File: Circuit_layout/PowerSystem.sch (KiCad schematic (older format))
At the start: 19 parts, among them U13 PDQ10-D, U14 PDQ15-D, U18 PDQ6-D

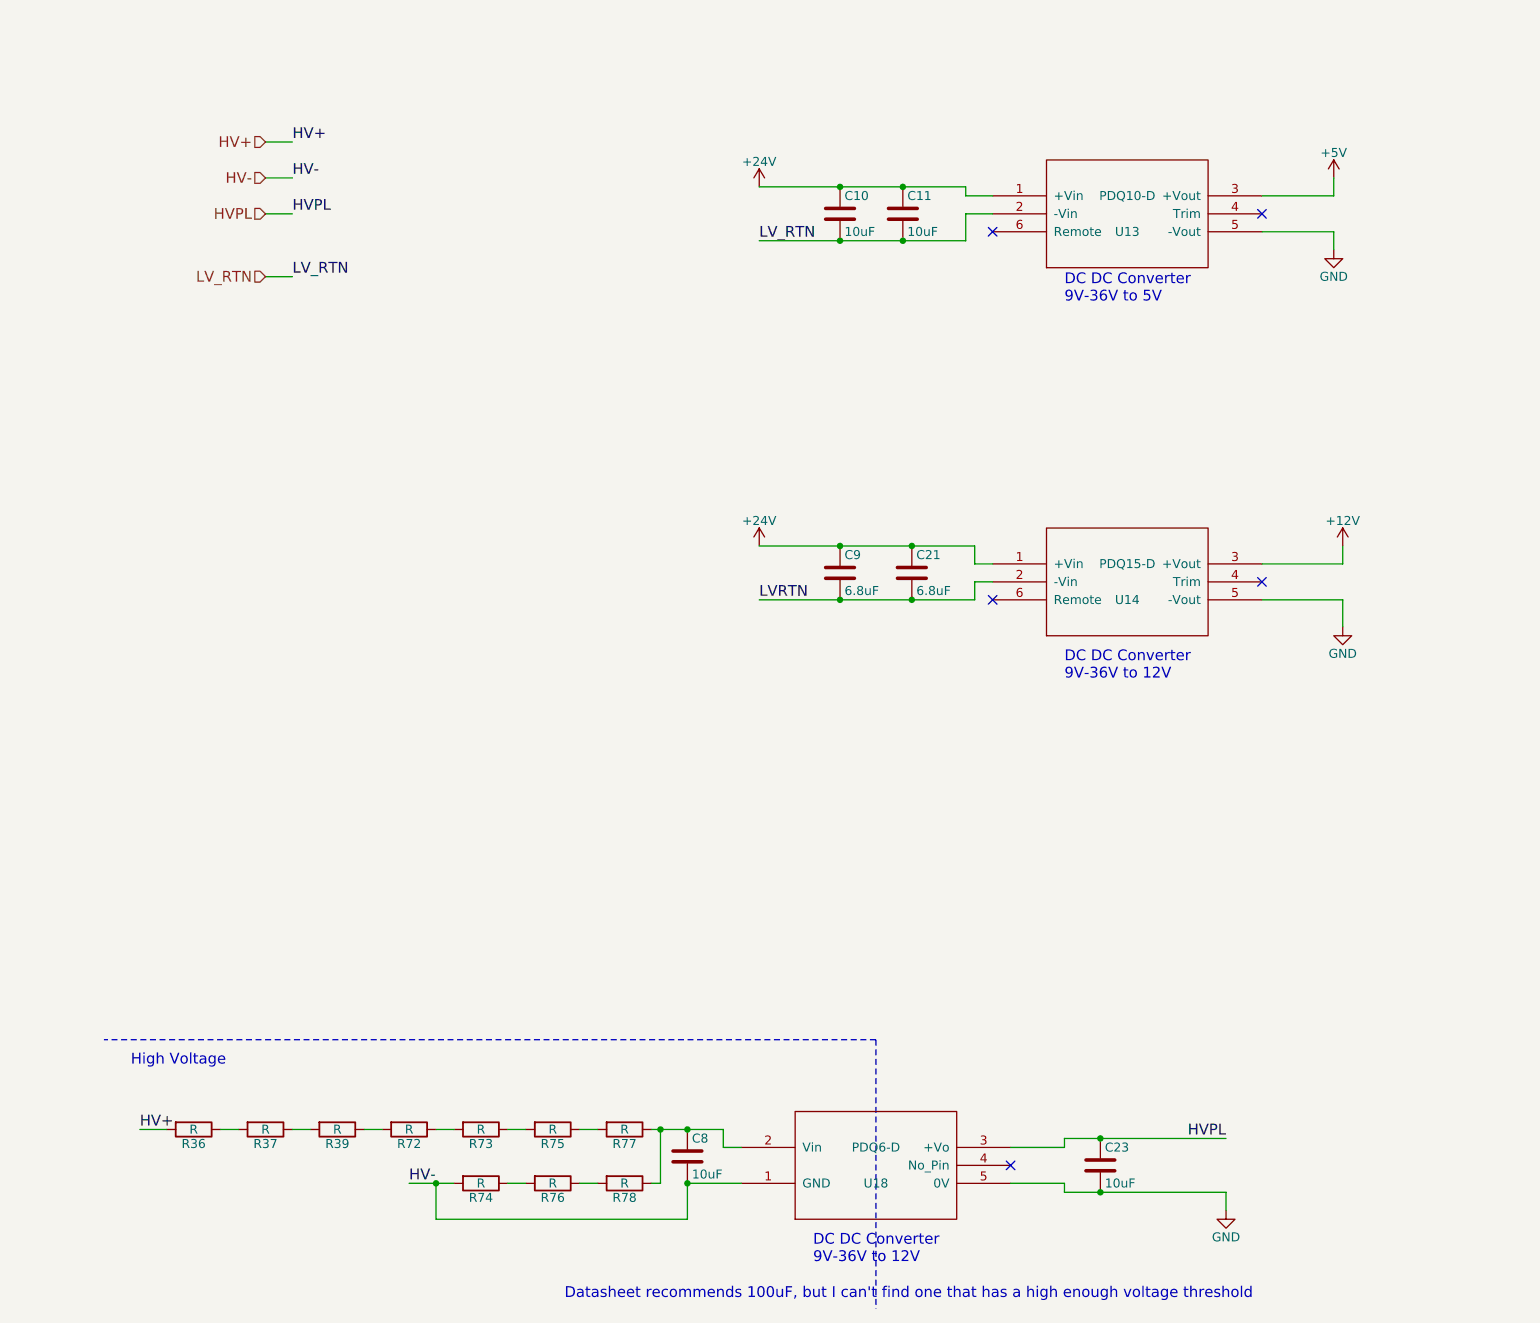
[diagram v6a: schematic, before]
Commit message: cleaned up sch, added bypass pass. no net warnings
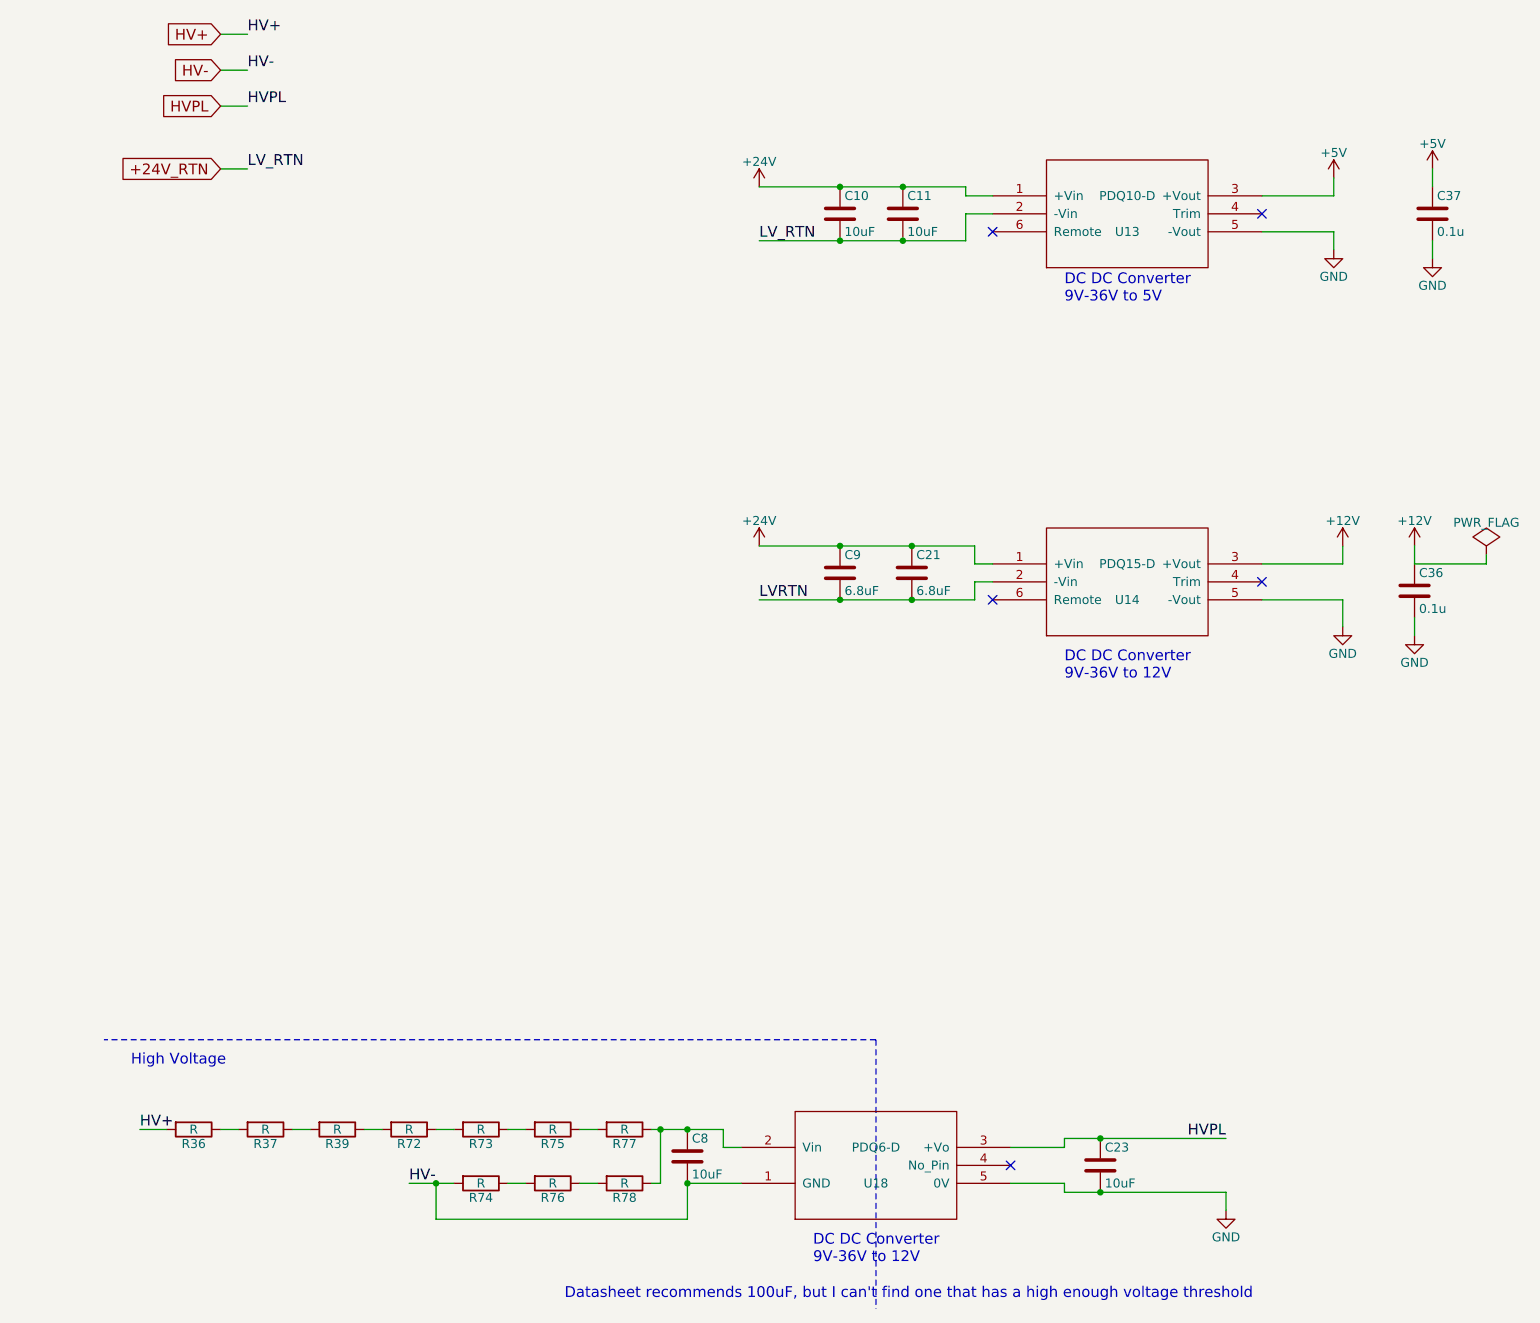
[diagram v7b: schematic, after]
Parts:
- added C36, C37: 0.1u, Capacitors_SMD:C_0805_HandSoldering, symbol C
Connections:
- net +12V: now also C36.1
- net +5V: now also C37.1
- net GND: now also C36.2, C37.2
- net LV_RTN renamed +24V_RTN
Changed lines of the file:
@@
 EESchema Schematic File Version 2
 LIBS:Circuit_layout-rescue
-LIBS:TSI_KiCad_Lib
 LIBS:TSI_HV_Isolater-cache
 LIBS:74xgxx
@@
 Connection ~ 4550 1550
 $Comp
-L +24V #PWR042
+L +24V #PWR43
 U 1 1 58AF1DB3
 P 4100 3550
-F 0 "#PWR042" H 4100 3400 50  0001 C CNN
+F 0 "#PWR43" H 4100 3400 50  0001 C CNN
 F 1 "+24V" H 4100 3690 50  0000 C CNN
 F 2 "" H 4100 3550 50  0000 C CNN
@@
 $EndComp
 $Comp
-L +24V #PWR043
+L +24V #PWR42
 U 1 1 58AF1DD3
 P 4100 1550
-F 0 "#PWR043" H 4100 1400 50  0001 C CNN
+F 0 "#PWR42" H 4100 1400 50  0001 C CNN
 F 1 "+24V" H 4100 1690 50  0000 C CNN
 F 2 "" H 4100 1550 50  0000 C CNN
@@
 	7300 1600 7300 1500
 $Comp
-L +5V #PWR044
+L +5V #PWR45
 U 1 1 58AF2067
 P 7300 1500
-F 0 "#PWR044" H 7300 1350 50  0001 C CNN
+F 0 "#PWR45" H 7300 1350 50  0001 C CNN
 F 1 "+5V" H 7300 1640 50  0000 C CNN
 F 2 "" H 7300 1500 50  0000 C CNN
@@
 $EndComp
 $Comp
-L +12V #PWR045
+L +12V #PWR47
 U 1 1 58AF208D
 P 7350 3550
-F 0 "#PWR045" H 7350 3400 50  0001 C CNN
+F 0 "#PWR47" H 7350 3400 50  0001 C CNN
 F 1 "+12V" H 7350 3690 50  0000 C CNN
 F 2 "" H 7350 3550 50  0000 C CNN
@@
 	7300 1800 7300 1900
 $Comp
-L GND #PWR046
+L GND #PWR46
 U 1 1 58AF2561
 P 7300 1900
-F 0 "#PWR046" H 7300 1650 50  0001 C CNN
+F 0 "#PWR46" H 7300 1650 50  0001 C CNN
 F 1 "GND" H 7300 1750 50  0000 C CNN
 F 2 "" H 7300 1900 50  0000 C CNN
@@
 	7350 3850 7350 4000
 $Comp
-L GND #PWR047
+L GND #PWR48
 U 1 1 58AF25AA
 P 7350 4000
-F 0 "#PWR047" H 7350 3750 50  0001 C CNN
+F 0 "#PWR48" H 7350 3750 50  0001 C CNN
 F 1 "GND" H 7350 3850 50  0000 C CNN
 F 2 "" H 7350 4000 50  0000 C CNN
@@
 Wire Wire Line
 	800  6800 650  6800
-Text HLabel 1350 1300 0    60   Input ~ 0
+Wire Wire Line
+	1100 700  1250 700
+Wire Wire Line
+	1100 900  1250 900
+Wire Wire Line
+	1100 1100 1250 1100
+Wire Wire Line
+	1100 1450 1250 1450
+Text Label 1250 700  0    60   ~ 0
 HV+
-Text HLabel 1350 1500 0    60   Input ~ 0
+Text Label 1250 900  0    60   ~ 0
 HV-
-Text HLabel 1350 1700 0    60   Input ~ 0
+Text Label 1250 1100 0    60   ~ 0
 HVPL
-Text HLabel 1350 2050 0    60   Input ~ 0
+Text Label 1250 1450 0    60   ~ 0
 LV_RTN
-Wire Wire Line
-	1350 1300 1500 1300
-Wire Wire Line
-	1350 1500 1500 1500
-Wire Wire Line
-	1350 1700 1500 1700
-Wire Wire Line
-	1350 2050 1500 2050
-Text Label 1500 1300 0    60   ~ 0
-HV+
-Text Label 1500 1500 0    60   ~ 0
-HV-
-Text Label 1500 1700 0    60   ~ 0
-HVPL
-Text Label 1500 2050 0    60   ~ 0
-LV_RTN
-$Comp
-L GND #PWR048
+$Comp
+L GND #PWR44
 U 1 1 58BA25F0
 P 6700 7250
-F 0 "#PWR048" H 6700 7000 50  0001 C CNN
+F 0 "#PWR44" H 6700 7000 50  0001 C CNN
 F 1 "GND" H 6700 7100 50  0000 C CNN
 F 2 "" H 6700 7250 50  0000 C CNN
@@
 Text Notes 600  6450 0    60   ~ 0
 High Voltage
+$Comp
+L C C37
+U 1 1 58B9D10D
+P 7850 1700
+F 0 "C37" H 7875 1800 50  0000 L CNN
+F 1 "0.1u" H 7875 1600 50  0000 L CNN
+F 2 "Capacitors_SMD:C_0805_HandSoldering" H 7888 1550 50  0001 C CNN
+F 3 "http://www.kemet.com/Lists/ProductCatalog/Attachments/53/KEM_C1002_X7R_SMD.pdf" H 7850 1700 50  0001 C CNN
+F 4 "399-1168-1-ND" H 7850 1700 60  0001 C CNN "Digikey P/N"
+F 5 "http://www.digikey.com/product-detail/en/kemet/C0805C104K3RACTU/399-1168-1-ND/411443" H 7850 1700 60  0001 C CNN "URL"
+F 6 "C0805C104K3RACTU" H 7850 1700 60  0001 C CNN "Man P/N"
+	1    7850 1700
+	1    0    0    -1
+$EndComp
+$Comp
+L GND #PWR52
+U 1 1 58B9D18E
+P 7850 1950
+F 0 "#PWR52" H 7850 1700 50  0001 C CNN
+F 1 "GND" H 7850 1800 50  0000 C CNN
+F 2 "" H 7850 1950 50  0000 C CNN
+F 3 "" H 7850 1950 50  0000 C CNN
+	1    7850 1950
+	1    0    0    -1
+$EndComp
+$Comp
+L +5V #PWR51
+U 1 1 58B9D1D5
+P 7850 1450
+F 0 "#PWR51" H 7850 1300 50  0001 C CNN
+F 1 "+5V" H 7850 1590 50  0000 C CNN
+F 2 "" H 7850 1450 50  0000 C CNN
+F 3 "" H 7850 1450 50  0000 C CNN
+	1    7850 1450
+	1    0    0    -1
+$EndComp
+Wire Wire Line
+	7850 1450 7850 1550
+Wire Wire Line
+	7850 1950 7850 1850
+$Comp
+L C C36
+U 1 1 58B9D39F
+P 7750 3800
+F 0 "C36" H 7775 3900 50  0000 L CNN
+F 1 "0.1u" H 7775 3700 50  0000 L CNN
+F 2 "Capacitors_SMD:C_0805_HandSoldering" H 7788 3650 50  0001 C CNN
+F 3 "http://www.kemet.com/Lists/ProductCatalog/Attachments/53/KEM_C1002_X7R_SMD.pdf" H 7750 3800 50  0001 C CNN
+F 4 "399-1168-1-ND" H 7750 3800 60  0001 C CNN "Digikey P/N"
+F 5 "http://www.digikey.com/product-detail/en/kemet/C0805C104K3RACTU/399-1168-1-ND/411443" H 7750 3800 60  0001 C CNN "URL"
+F 6 "C0805C104K3RACTU" H 7750 3800 60  0001 C CNN "Man P/N"
+	1    7750 3800
+	1    0    0    -1
+$EndComp
+$Comp
+L GND #PWR50
+U 1 1 58B9D3A5
+P 7750 4050
+F 0 "#PWR50" H 7750 3800 50  0001 C CNN
+F 1 "GND" H 7750 3900 50  0000 C CNN
+F 2 "" H 7750 4050 50  0000 C CNN
+F 3 "" H 7750 4050 50  0000 C CNN
+	1    7750 4050
+	1    0    0    -1
+$EndComp
+Wire Wire Line
+	7750 3550 7750 3650
+Wire Wire Line
+	7750 4050 7750 3950
+$Comp
+L +12V #PWR49
+U 1 1 58B9D62A
+P 7750 3550
+F 0 "#PWR49" H 7750 3400 50  0001 C CNN
+F 1 "+12V" H 7750 3690 50  0000 C CNN
+F 2 "" H 7750 3550 50  0000 C CNN
+F 3 "" H 7750 3550 50  0000 C CNN
+	1    7750 3550
+	1    0    0    -1
+$EndComp
+$Comp
+L PWR_FLAG #FLG3
+U 1 1 58B9E33D
+P 8150 3600
+F 0 "#FLG3" H 8150 3695 50  0001 C CNN
+F 1 "PWR_FLAG" H 8150 3780 50  0000 C CNN
+F 2 "" H 8150 3600 50  0000 C CNN
+F 3 "" H 8150 3600 50  0000 C CNN
+	1    8150 3600
+	1    0    0    -1
+$EndComp
+Wire Wire Line
+	7750 3650 8150 3650
+Wire Wire Line
+	8150 3650 8150 3600
+Text GLabel 1100 700  0    60   Input ~ 0
+HV+
+Text GLabel 1100 900  0    60   Input ~ 0
+HV-
+Text GLabel 1100 1100 0    60   Input ~ 0
+HVPL
+Text GLabel 1100 1450 0    60   Input ~ 0
++24V_RTN
 $EndSCHEMATC

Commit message: took notes on nadovich's proposed changes
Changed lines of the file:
@@
 	5400 3650 5300 3650
 Wire Wire Line
-	5300 3650 5300 3550
-Wire Wire Line
-	5300 3550 4100 3550
+	5300 3550 5300 3650
+Wire Wire Line
+	4100 3550 5300 3550
 Connection ~ 4950 3550
 Connection ~ 4550 3550
@@
 	5400 3750 5300 3750
 Wire Wire Line
-	5300 3750 5300 3850
-Wire Wire Line
-	5300 3850 4100 3850
+	5300 3850 5300 3750
+Wire Wire Line
+	4100 3850 5300 3850
 Connection ~ 4950 3850
 Connection ~ 4550 3850
@@
 	5400 1600 5250 1600
 Wire Wire Line
-	5250 1600 5250 1550
+	5250 1550 5250 1600
 Wire Wire Line
 	5400 1700 5250 1700
 Wire Wire Line
-	5250 1700 5250 1850
-Wire Wire Line
-	5250 1850 4100 1850
+	5250 1850 5250 1700
+Wire Wire Line
+	4100 1850 5250 1850
 Connection ~ 4900 1550
 Connection ~ 4900 1850
@@
 	4000 6900 3900 6900
 Wire Wire Line
-	3900 6900 3900 6800
-Wire Wire Line
-	3900 6800 3500 6800
+	3900 6800 3900 6900
+Wire Wire Line
+	3500 6800 3900 6800
 Connection ~ 3700 6800
 Connection ~ 3700 7100
@@
 	6700 7150 6700 7250
 Wire Wire Line
-	5250 1550 4100 1550
+	4100 1550 5250 1550
 Wire Notes Line
 	4750 6300 4750 7800
@@
 $EndComp
 Wire Wire Line
-	7750 3550 7750 3650
+	7750 3300 7750 3650
 Wire Wire Line
 	7750 4050 7750 3950
@@
 L +12V #PWR49
 U 1 1 58B9D62A
-P 7750 3550
-F 0 "#PWR49" H 7750 3400 50  0001 C CNN
-F 1 "+12V" H 7750 3690 50  0000 C CNN
-F 2 "" H 7750 3550 50  0000 C CNN
-F 3 "" H 7750 3550 50  0000 C CNN
-	1    7750 3550
+P 7750 3300
+F 0 "#PWR49" H 7750 3150 50  0001 C CNN
+F 1 "+12V" H 7750 3440 50  0000 C CNN
+F 2 "" H 7750 3300 50  0000 C CNN
+F 3 "" H 7750 3300 50  0000 C CNN
+	1    7750 3300
 	1    0    0    -1
 $EndComp
@@
 L PWR_FLAG #FLG3
 U 1 1 58B9E33D
-P 8150 3600
-F 0 "#FLG3" H 8150 3695 50  0001 C CNN
-F 1 "PWR_FLAG" H 8150 3780 50  0000 C CNN
-F 2 "" H 8150 3600 50  0000 C CNN
-F 3 "" H 8150 3600 50  0000 C CNN
-	1    8150 3600
-	1    0    0    -1
-$EndComp
-Wire Wire Line
-	7750 3650 8150 3650
-Wire Wire Line
-	8150 3650 8150 3600
+P 8150 3300
+F 0 "#FLG3" H 8150 3395 50  0001 C CNN
+F 1 "PWR_FLAG" H 8150 3480 50  0000 C CNN
+F 2 "" H 8150 3300 50  0000 C CNN
+F 3 "" H 8150 3300 50  0000 C CNN
+	1    8150 3300
+	1    0    0    -1
+$EndComp
 Text GLabel 1100 700  0    60   Input ~ 0
 HV+
@@
 Text GLabel 1100 1450 0    60   Input ~ 0
 +24V_RTN
+Wire Wire Line
+	8150 3300 8150 3500
+Wire Wire Line
+	8150 3500 7750 3500
+Connection ~ 7750 3500
 $EndSCHEMATC
